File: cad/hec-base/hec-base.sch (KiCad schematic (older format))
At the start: 3 parts, among them J101 Micromatch 12p, J102 Micromatch 10p, J103 Micromatch 8p

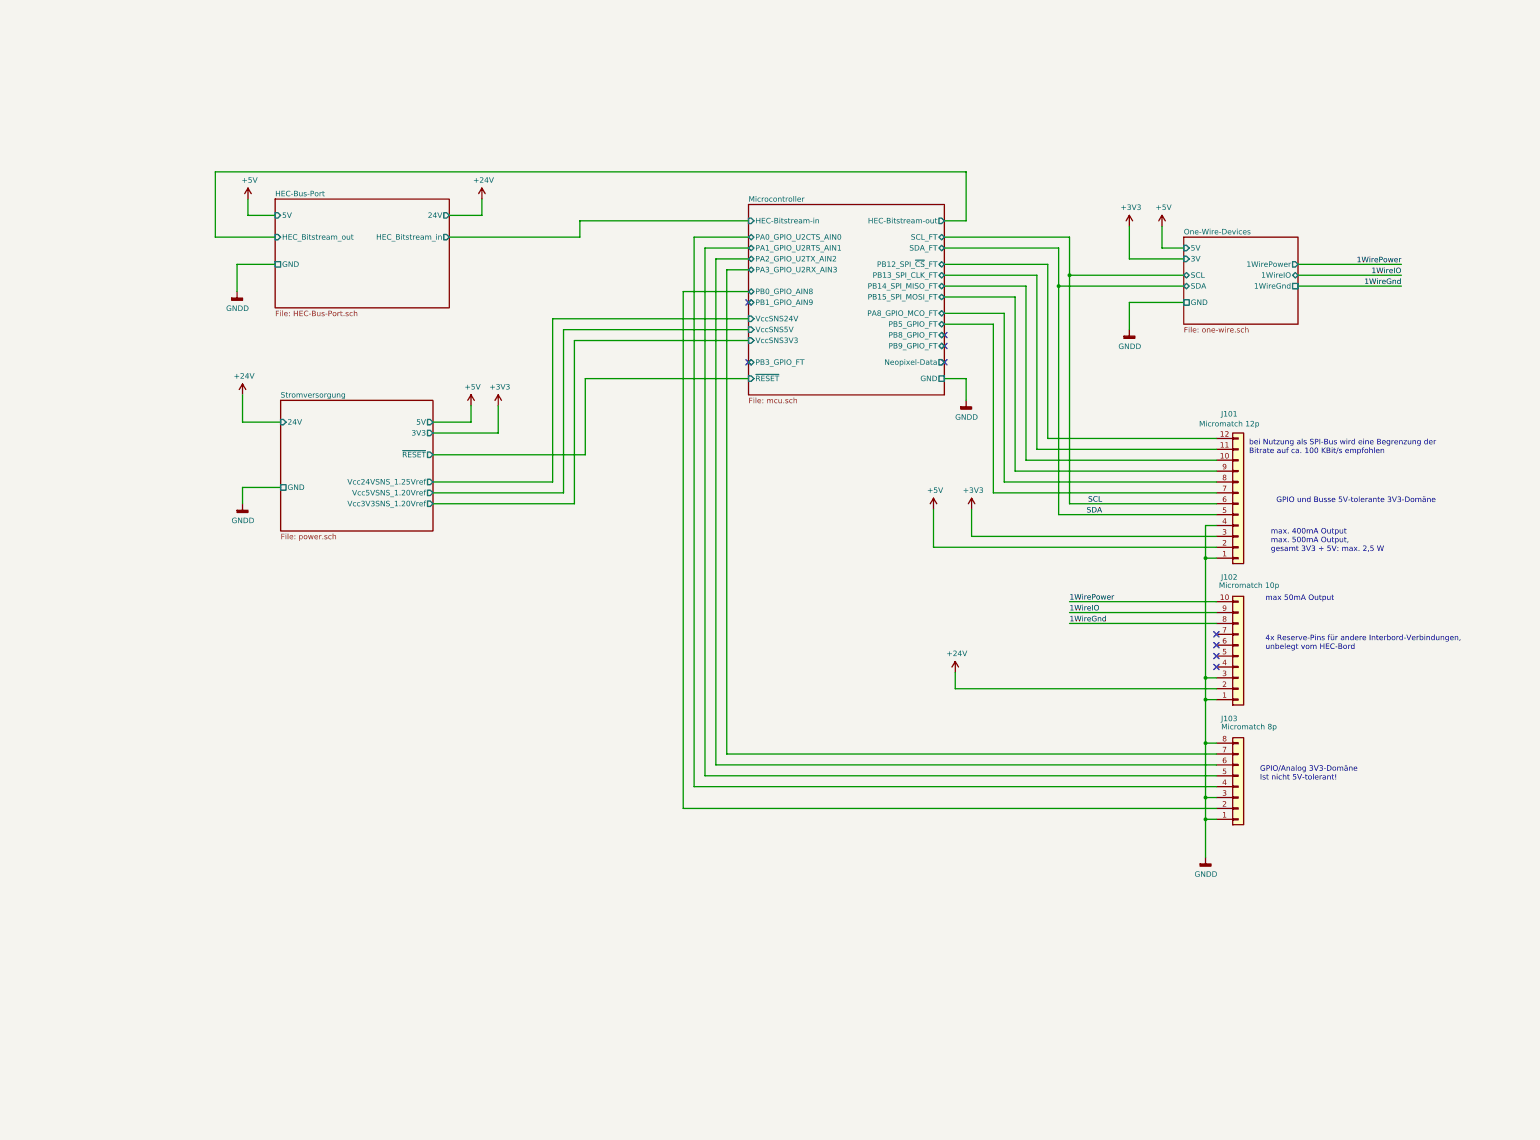
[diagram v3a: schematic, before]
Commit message: Entflochtene Leiterplatte mit Schaltplan speichern.
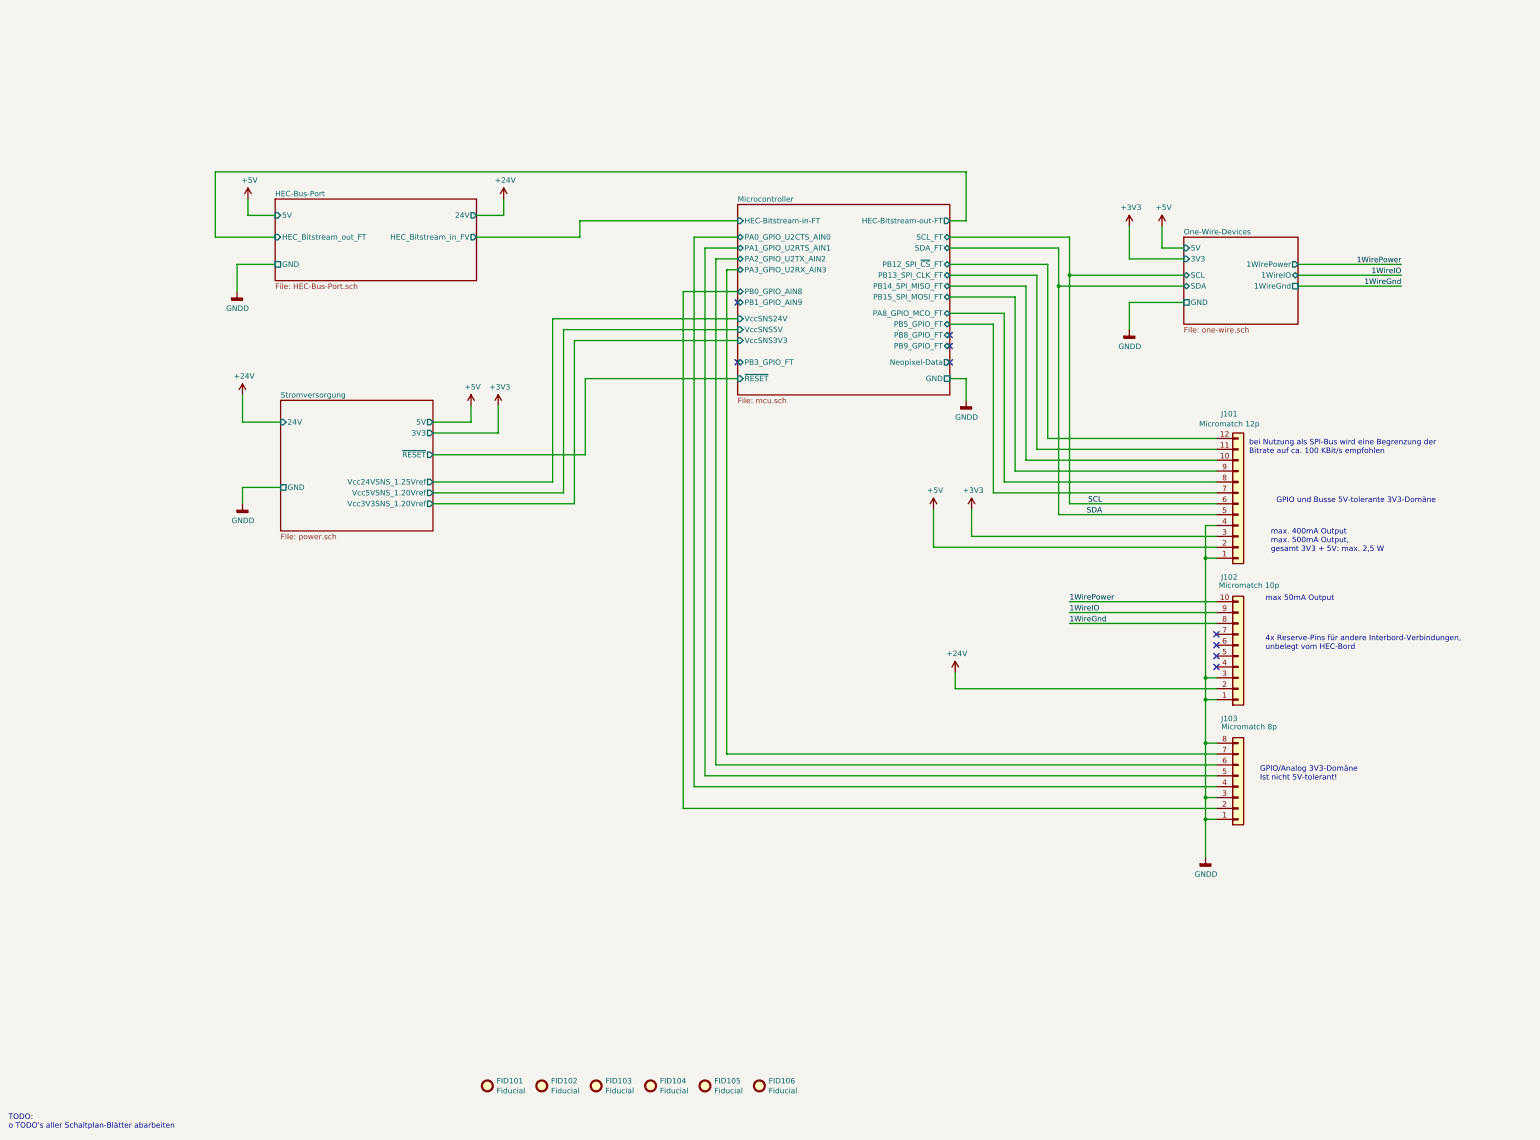
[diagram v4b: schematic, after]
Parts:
- added FID101, FID102, FID103, FID104, FID105, FID106: Fiducial, Fiducial:Fiducial_0.5mm_Mask1mm, symbol Mechanical:Fiducial
- J102: footprint Connectors_MicroMatch_MT:ConnectorMicromatch-10-SMD-polarized -> Connectors_MicroMatch_MT:ConnectorMicromatch-10-horizontal-THT
- J103: footprint Connectors_MicroMatch_MT:ConnectorMicromatch-8-horizontal-THT -> Connectors_MicroMatch_MT:ConnectorMicromatch-8-SMD-polarized
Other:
- note added: "TODO:\no TODO's aller Schaltplan-Blätter abarbeiten\n"
